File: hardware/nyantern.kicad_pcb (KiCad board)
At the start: 2 copper layers, 100 x 100 mm, 10 parts

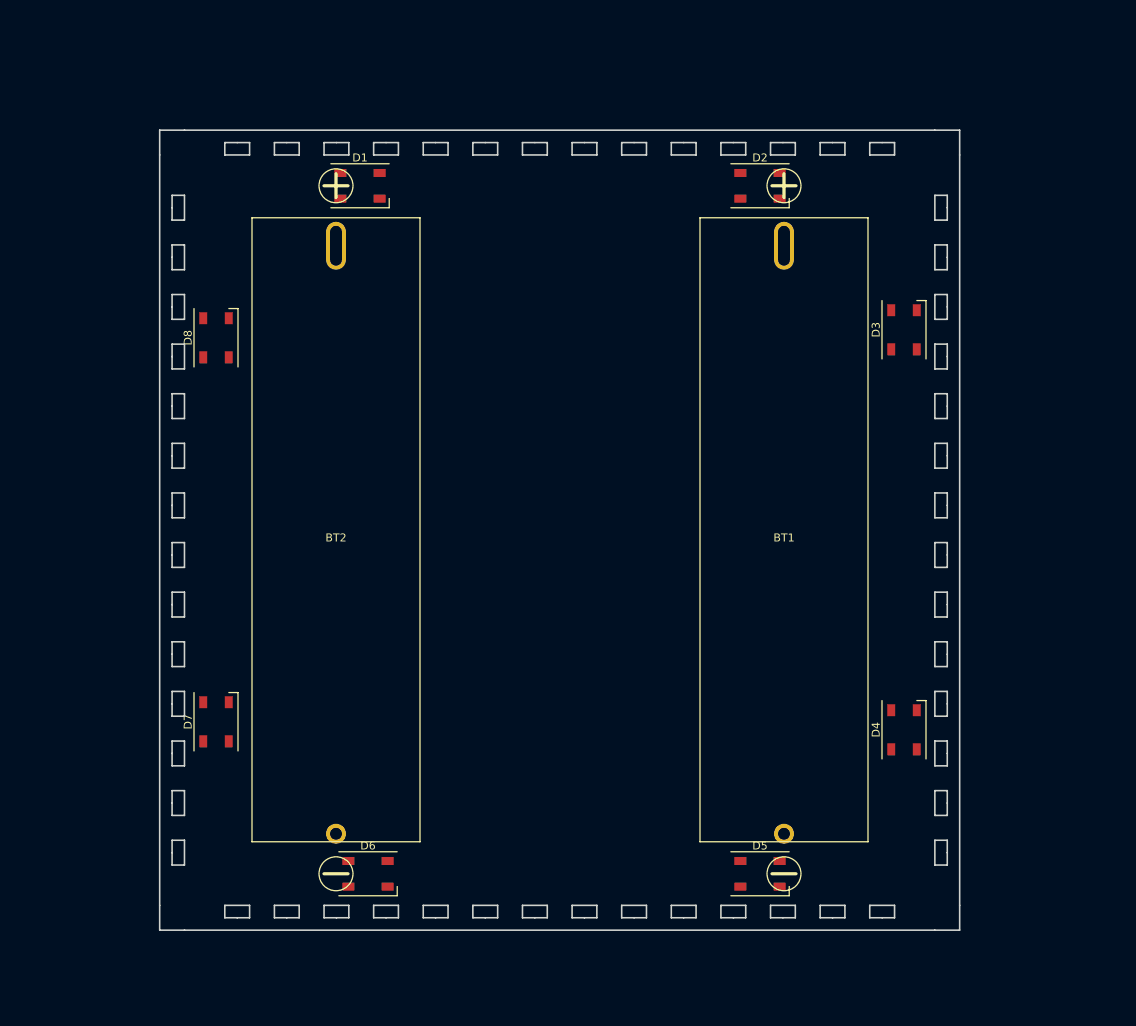
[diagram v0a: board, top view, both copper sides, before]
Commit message: Made footprints for modules and put everything on the board
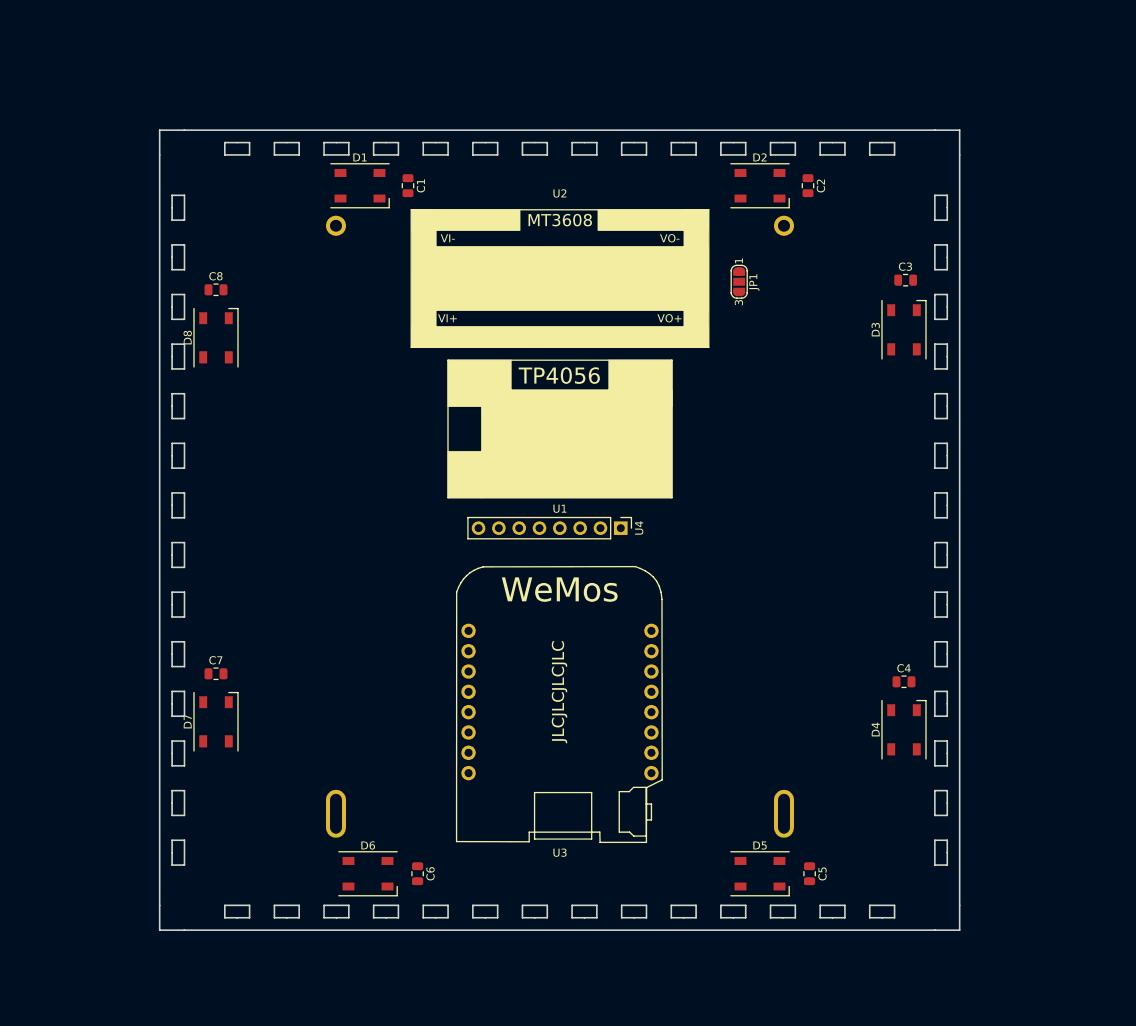
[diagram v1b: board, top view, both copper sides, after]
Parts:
- added C1: C_Small, Capacitor_SMD:C_0805_2012Metric, F.Cu at (131.0, 57.0)
- added C2: C_Small, Capacitor_SMD:C_0805_2012Metric, F.Cu at (181.0, 57.0)
- added C3: C_Small, Capacitor_SMD:C_0805_2012Metric, F.Cu at (193.2, 68.8)
- added C4: C_Small, Capacitor_SMD:C_0805_2012Metric, F.Cu at (193.0, 119.0)
- added C5: C_Small, Capacitor_SMD:C_0805_2012Metric, F.Cu at (181.2, 143.0)
- added C6: C_Small, Capacitor_SMD:C_0805_2012Metric, F.Cu at (132.2, 143.0)
- added C7: C_Small, Capacitor_SMD:C_0805_2012Metric, F.Cu at (107.0, 118.0)
- added C8: C_Small, Capacitor_SMD:C_0805_2012Metric, F.Cu at (107.0, 70.0)
- added JP1: SolderJumper_3_Open, Jumper:SolderJumper-3_P1.3mm_Open_RoundedPad1.0x1.5mm_NumberLabels, F.Cu at (172.4, 69.0)
- added U1: TP4056board, BamboulabFootprints:TP4056board, F.Cu at (150.0, 87.4)
- added U2: MT3608board, BamboulabFootprints:MT3608board, F.Cu at (150.0, 68.6)
- added U3: WeMos_mini, BamboulabFootprints:D1_mini_board, F.Cu at (150.0, 122.8)
- added U4: MPU6050board, Connector_PinHeader_2.54mm:PinHeader_1x08_P2.54mm_Vertical, F.Cu at (157.6, 99.8)
- BT1, BT2: moved to B.Cu
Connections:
- BT2 pad 1: Net-(BT2-Pad1) -> Net-(BT1-Pad1)
- BT2 pad 2: Net-(BT2-Pad2) -> Net-(BT1-Pad2)
- D1 pad 1: Net-(D1-Pad1) -> Vdrive
- D1 pad 2: Net-(D1-Pad2) -> SK2812
- D1 pad 3: Net-(D1-Pad3) -> GND
- D2 pad 1: Net-(D2-Pad1) -> Vdrive
- D2 pad 2: Net-(D2-Pad2) -> Net-(D1-Pad4)
- D2 pad 3: Net-(D2-Pad3) -> GND
- D3 pad 1: Net-(D3-Pad1) -> Vdrive
- D3 pad 2: Net-(D3-Pad2) -> Net-(D2-Pad4)
- D3 pad 3: Net-(D3-Pad3) -> GND
- D4 pad 1: Net-(D4-Pad1) -> Vdrive
- D4 pad 2: Net-(D4-Pad2) -> Net-(D3-Pad4)
- D4 pad 3: Net-(D4-Pad3) -> GND
- D5 pad 1: Net-(D5-Pad1) -> Vdrive
- D5 pad 2: Net-(D5-Pad2) -> Net-(D4-Pad4)
- D5 pad 3: Net-(D5-Pad3) -> GND
- D6 pad 1: Net-(D6-Pad1) -> Vdrive
- D6 pad 2: Net-(D6-Pad2) -> Net-(D5-Pad4)
- D6 pad 3: Net-(D6-Pad3) -> GND
- D7 pad 1: Net-(D7-Pad1) -> Vdrive
- D7 pad 2: Net-(D7-Pad2) -> Net-(D6-Pad4)
- D7 pad 3: Net-(D7-Pad3) -> GND
- D8 pad 1: Net-(D8-Pad1) -> Vdrive
- D8 pad 2: Net-(D8-Pad2) -> Net-(D7-Pad4)
- D8 pad 3: Net-(D8-Pad3) -> GND
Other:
- board text added: "JLCJLCJLCJLC"

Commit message: First version of the board laid, added monting holes and duplicaded some leds to test out more centered light source
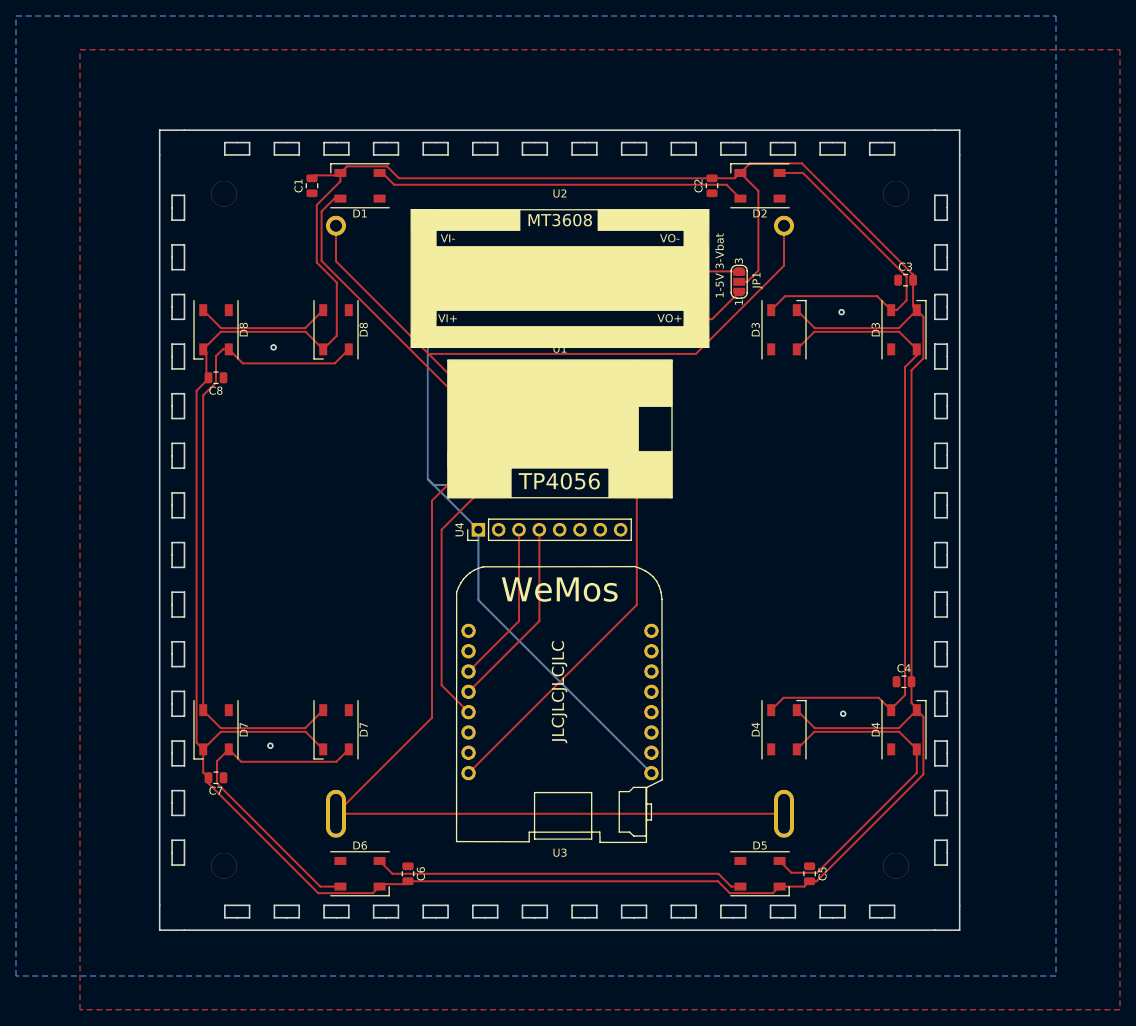
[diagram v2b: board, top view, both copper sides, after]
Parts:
- added D3: SK6812, LED_SMD:LED_SK6812_PLCC4_5.0x5.0mm_P3.2mm, F.Cu at (178.0, 75.0)
- added D4: SK6812, LED_SMD:LED_SK6812_PLCC4_5.0x5.0mm_P3.2mm, F.Cu at (178.0, 125.0)
- added D7: SK6812, LED_SMD:LED_SK6812_PLCC4_5.0x5.0mm_P3.2mm, F.Cu at (122.0, 125.0)
- added D8: SK6812, LED_SMD:LED_SK6812_PLCC4_5.0x5.0mm_P3.2mm, F.Cu at (122.0, 75.0)
- added REF**: MountingHole_3.2mm_M3, MountingHole:MountingHole_3.2mm_M3, F.Cu at (192.0, 142.0)
- added REF**: MountingHole_3.2mm_M3, MountingHole:MountingHole_3.2mm_M3, F.Cu at (108.0, 142.0)
- added REF**: MountingHole_3.2mm_M3, MountingHole:MountingHole_3.2mm_M3, F.Cu at (108.0, 58.0)
- added REF**: MountingHole_3.2mm_M3, MountingHole:MountingHole_3.2mm_M3, F.Cu at (192.0, 58.0)
- moved U4 17.8 mm to (139.8, 100.0), turned to 90 degrees
- moved C7 13.0 mm to (107.0, 131.0), turned to 180 degrees
- moved C1 12.0 mm to (119.0, 57.0), turned to 90 degrees
- moved C2 12.0 mm to (169.0, 57.0), turned to 90 degrees
- moved C8 11.0 mm to (107.0, 81.0), turned to 180 degrees
- moved C6 1.20 mm to (131.0, 143.0)
- moved D6 1.00 mm to (125.0, 143.0)
- moved D7 1.00 mm to (107.0, 125.0), turned to 270 degrees
- moved D8 1.00 mm to (107.0, 75.0), turned to 270 degrees
- turned D1 to 180 degrees
- turned D2 to 180 degrees
- turned JP1 to 90 degrees
- turned U1 to 180 degrees
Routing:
- net Vdrive: track 0.00 -> 413.7 mm
- net +BATT: track 0.00 -> 114.9 mm
- net Net-(BT1-Pad1): track 0.00 -> 106.5 mm
- net Net-(BT1-Pad2): track 0.00 -> 81.8 mm
- net Net-(D7-Pad4): track 0.00 -> 80.2 mm
- net Net-(D3-Pad4): track 0.00 -> 79.5 mm
- net SK2812: track 0.00 -> 77.5 mm
- net +5V: track 0.00 -> 59.5 mm
- net Net-(D5-Pad4): track 0.00 -> 46.4 mm
- net Net-(D1-Pad4): track 0.00 -> 46.4 mm
- net Net-(D2-Pad4): track 0.00 -> 43.1 mm
- net Net-(D4-Pad4): track 0.00 -> 42.7 mm
- net Net-(D6-Pad4): track 0.00 -> 41.9 mm
- net SDA: track 0.00 -> 23.9 mm
- net SCL: track 0.00 -> 20.3 mm
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- added copper zone on B.Cu, net GND
- added copper zone on F.Cu, net GND
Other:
- board text added: "1-5V 3-Vbat"

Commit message: resized the board and removed box.py slots, swapped location of battery charging/boost, rounded corners, all yours Gboi
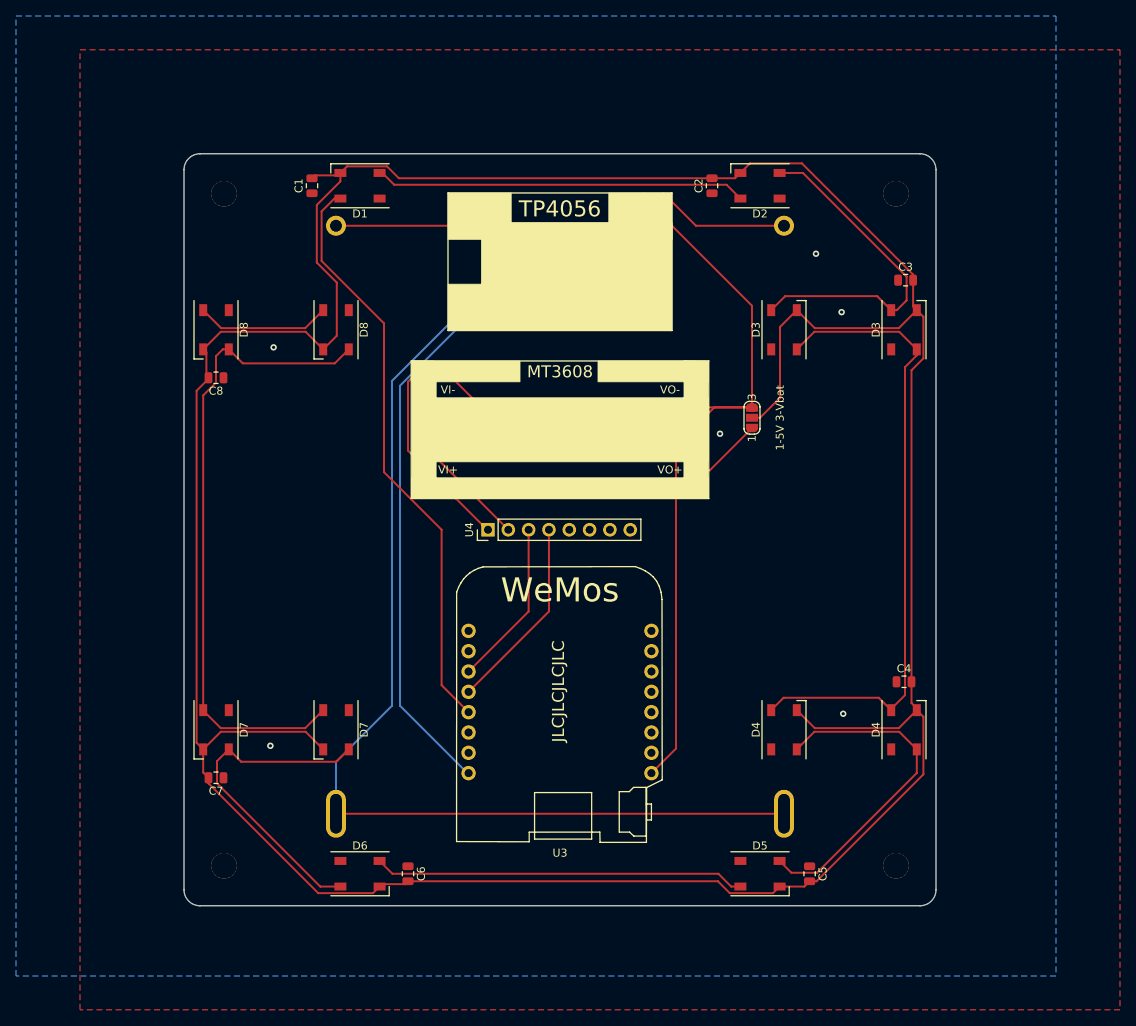
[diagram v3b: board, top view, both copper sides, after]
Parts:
- moved U1 20.9 mm to (150.0, 66.5), turned to 0 degrees
- moved e 18.9 mm to (150.0, 87.5)
- moved JP1 17.1 mm to (174.0, 86.0)
- moved U4 1.20 mm to (141.0, 100.0)
- renumbered U2 to e
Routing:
- net Net-(BT1-Pad1): track 106.5 -> 153.5 mm
- net +BATT: track 114.9 -> 152.3 mm
- net GND: track 0.00 -> 21.7 mm, vias 4 -> 6
- net Net-(BT1-Pad2): track 81.8 -> 70.3 mm
- net +5V: track 59.5 -> 64.1 mm
- net SK2812: track 77.5 -> 73.2 mm
- net Net-(JP1-Pad1): track 7.29 -> 9.68 mm
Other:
- board size 100 x 100 mm -> 94 x 94 mm

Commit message: Mechanical integration of PCB, added pegs and holes on PCB
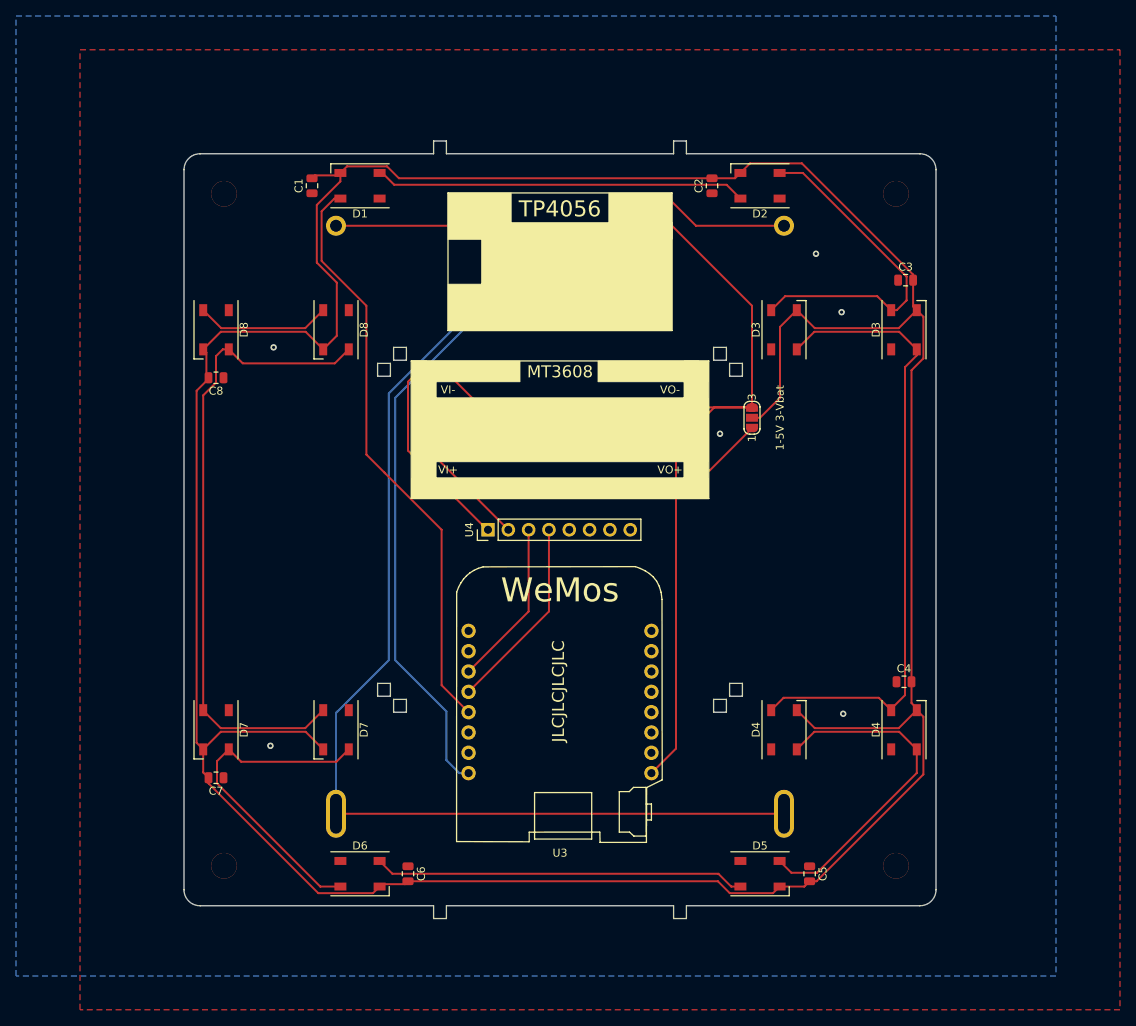
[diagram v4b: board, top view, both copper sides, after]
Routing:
- net +5V: track 64.1 -> 65.3 mm
- net Net-(BT1-Pad1): track 153.5 -> 154.2 mm
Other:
- board size 94 x 94 mm -> 94 x 97.2 mm
